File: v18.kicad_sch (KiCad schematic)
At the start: 58 parts

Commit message: More work in progres
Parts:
- added C? (x2): C, symbol Device:C
- C521, C541: renamed from C?; now not fitted
- L53, L54, L55: renamed from L?; value L_Ferrite_Power -> 100
- gave numbers to parts that had none: 53
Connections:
- net PGND is gone; now on net GNDPWR: C501.2, C502.1, C503.1, C504.2, C511.1, C512.2, C513.1, C521.2, C522.1, C523.1, C524.1, C525.1, C526.1, C527.1, C528.1, C529.1, C530.1, C541.1, C542.2, C543.2, C544.1, C545.1, C547.1, C548.1, C549.1, C550.1, C551.1, R502.2, R504.2, R521.2, R522.2, R523.2, R542.2, R543.2, U51.19 (PGND), U52.17 (NC), U52.18 (NC), U52.19 (NC), U52.21 (EP), U52.4 (6.4V), U52.5 (6.4V), U52.6 (3.2V), U52.7 (GND), U53.10 (NC), U53.11 (NC), U53.12 (NC), U53.17 (NC), U53.18 (NC), U53.19 (NC), U53.21 (EP), U53.4 (NC), U53.5 (NC), U53.6 (NC), U53.7 (GND), U53.8 (NC), U53.9 (NC)
- net at R511.1, U51.10 (COMP2): now also C?.2
- net at R501.1, U51.6 (COMP1): now also C?.2
- net GNDPWR: now reaches L52.2
- net GNDPWR: now also C?.1, C?.1
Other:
- moved on the sheet: C501, C522, C523, L53, R501, R511

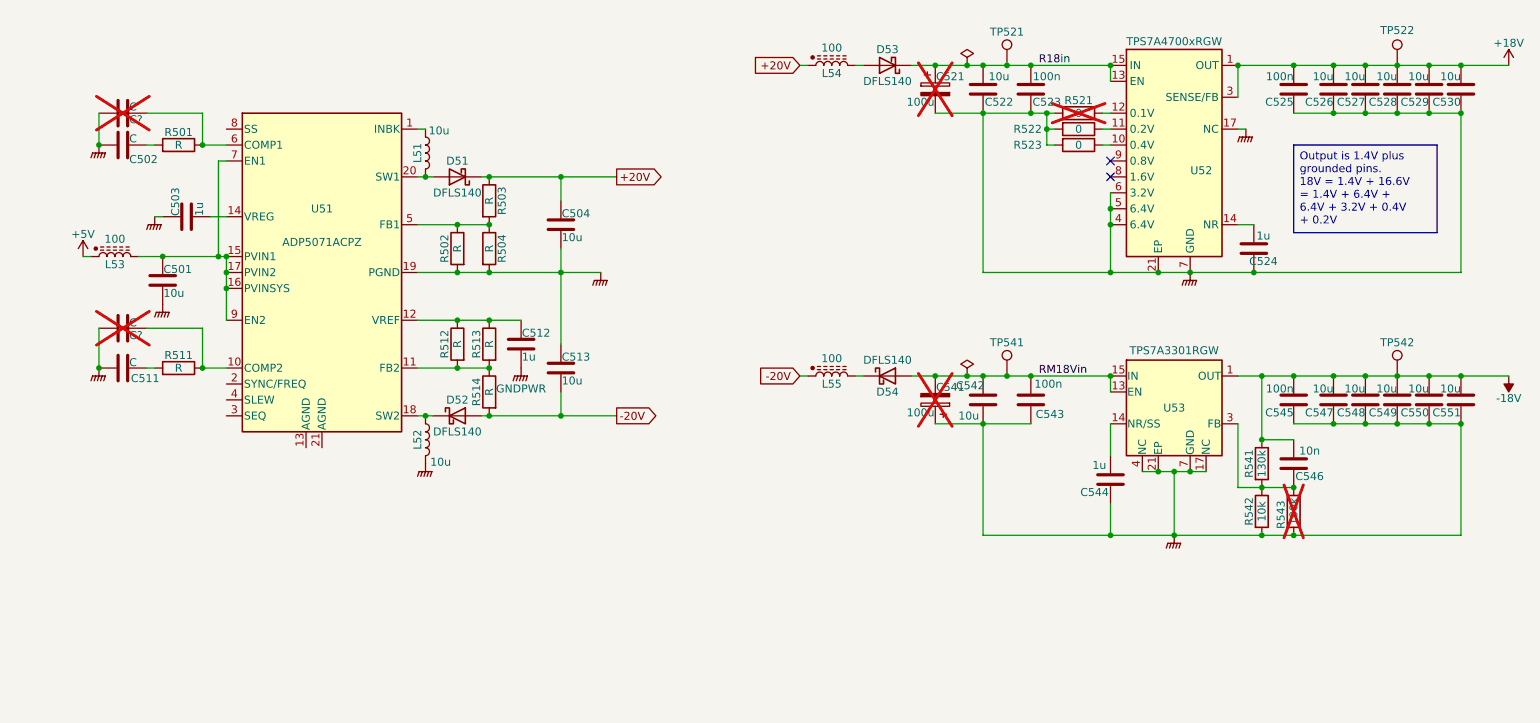
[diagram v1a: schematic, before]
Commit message: Analog side is more or less complete.
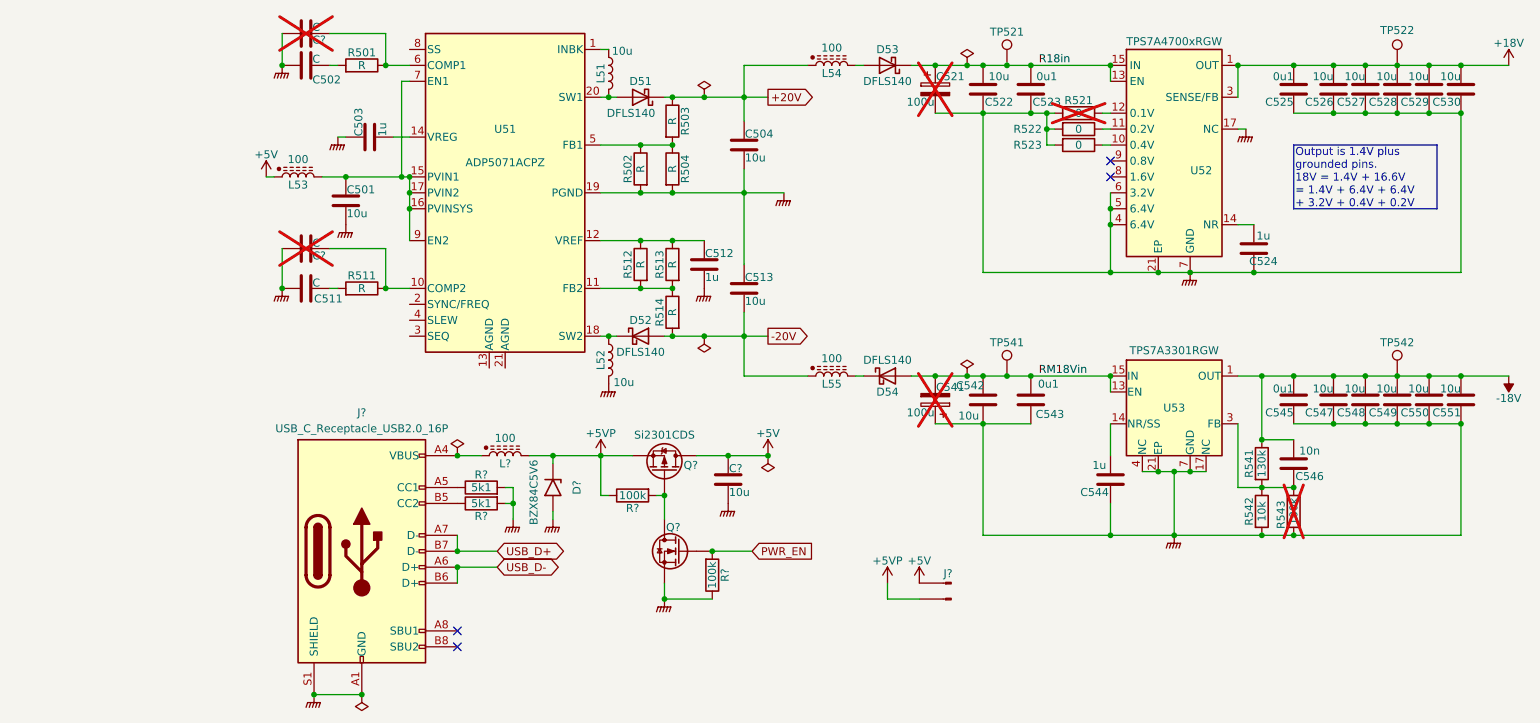
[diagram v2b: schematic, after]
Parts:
- added C?: 10u, symbol Device:C
- added D?: BZX84C5V6, Package_TO_SOT_SMD:SOT-23, symbol Parts:BZX84Cxx
- added J?: Conn_01x02_Pin, symbol Connector:Conn_01x02_Pin
- added J?: USB_C_Receptacle_USB2.0_16P, symbol Connector:USB_C_Receptacle_USB2.0_16P
- added L?: 100, symbol Parts:L_Ferrite_Power
- added Q?: Si2301CDS, Package_TO_SOT_SMD:SOT-23, symbol External:Si2301CDS
- added Q?: AO3400A, Package_TO_SOT_SMD:SOT-23, symbol Transistor_FET:AO3400A
- added R? (x2): 5k1, symbol Device:R
- added R? (x2): 100k, symbol Device:R
- C523, C525, C543, C545: value 100n -> 0u1
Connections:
- net +5V: now also C?.1, J?.2 (Pin_2), Q?.3 (D)
- net GNDPWR: now also C?.2, D?.1 (A), J?.A1 (GND), J?.A12 (GND), J?.B1 (GND), J?.B12 (GND), J?.S1 (SHIELD), Q?.2 (S), R?.1, R?.2, R?.2
- new net: Q?.1 (G), Q?.3 (D), R?.2
- new net: J?.A5 (CC1), R?.1
- new net: J?.B5 (CC2), R?.1
- new net: J?.A4 (VBUS), J?.A9 (VBUS), J?.B4 (VBUS), J?.B9 (VBUS), L?.1
- new net +5VP: D?.3 (K), J?.1 (Pin_1), L?.2, Q?.2 (S), R?.1
- new net PWR_EN: Q?.1 (G), R?.2
- new net USB_D+: J?.A7 (D-), J?.B7 (D-)
- new net USB_D-: J?.A6 (D+), J?.B6 (D+)
- no-connect marks 2 -> 4
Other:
- moved on the sheet: C501, C502, C503, C504, C511, C512, C513, C?, D51, D52, L51, L52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

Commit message: Little simplifications etc.
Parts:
- gave numbers to parts that had none: 11
- renumbered TP521 to TP51, TP522 to TP52, TP541 to TP53, TP542 to TP54
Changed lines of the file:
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@@
 		(on_board yes)
 		(dnp no)
-		(property "Reference" "TP541"
+		(property "Reference" "TP53"
 			(at 176.53 87.376 0)
 			(effects
@@
 			(project "lincal"
 				(path "/b054cef4-39e3-49d8-aff0-7ba5a206c187/79d139b8-187a-44f5-bd99-1da7793824c6"
-					(reference "TP541")
+					(reference "TP53")
 					(unit 1)
 				)
@@
 		(on_board yes)
 		(dnp no)
-		(property "Reference" "Q?"
+		(property "Reference" "Q51"
 			(at 124.968 106.934 90)
 			(effects
@@
 			(project ""
 				(path "/b054cef4-39e3-49d8-aff0-7ba5a206c187/79d139b8-187a-44f5-bd99-1da7793824c6"
-					(reference "Q?")
+					(reference "Q51")
 					(unit 1)
 				)
@@
 		(on_board yes)
 		(dnp no)
-		(property "Reference" "TP542"
+		(property "Reference" "TP54"
 			(at 238.76 87.376 0)
 			(effects
@@
 			(project "lincal"
 				(path "/b054cef4-39e3-49d8-aff0-7ba5a206c187/79d139b8-187a-44f5-bd99-1da7793824c6"
-					(reference "TP542")
+					(reference "TP54")
 					(unit 1)
 				)
@@
 		(on_board yes)
 		(dnp no)
-		(property "Reference" "R?"
+		(property "Reference" "R561"
 			(at 92.71 108.458 90)
 			(effects
@@
 			(project "lincal"
 				(path "/b054cef4-39e3-49d8-aff0-7ba5a206c187/79d139b8-187a-44f5-bd99-1da7793824c6"
-					(reference "R?")
+					(reference "R561")
 					(unit 1)
 				)
@@
 		(on_board yes)
 		(dnp no)
-		(property "Reference" "TP522"
+		(property "Reference" "TP52"
 			(at 238.76 37.592 0)
 			(effects
@@
 			(project "lincal"
 				(path "/b054cef4-39e3-49d8-aff0-7ba5a206c187/79d139b8-187a-44f5-bd99-1da7793824c6"
-					(reference "TP522")
+					(reference "TP52")
 					(unit 1)
 				)
@@
 		(on_board yes)
 		(dnp no)
-		(property "Reference" "R?"
+		(property "Reference" "R563"
 			(at 116.84 113.792 90)
 			(effects
@@
 			(project "lincal"
 				(path "/b054cef4-39e3-49d8-aff0-7ba5a206c187/79d139b8-187a-44f5-bd99-1da7793824c6"
-					(reference "R?")
+					(reference "R563")
 					(unit 1)
 				)
@@
 		(on_board yes)
 		(dnp no)
-		(property "Reference" "R?"
+		(property "Reference" "R562"
 			(at 92.71 115.062 90)
 			(effects
@@
 			(project "lincal"
 				(path "/b054cef4-39e3-49d8-aff0-7ba5a206c187/79d139b8-187a-44f5-bd99-1da7793824c6"
-					(reference "R?")
+					(reference "R562")
 					(unit 1)
 				)
@@
 		(dnp no)
 		(property "Reference" "C543"
-			(at 183.388 98.806 0)
+			(at 180.34 98.552 0)
 			(effects
 				(font
 					(size 1.27 1.27)
 				)
+				(justify right)
 			)
 		)
 		(property "Value" "0u1"
-			(at 183.134 93.98 0)
+			(at 180.34 94.488 0)
 			(effects
 				(font
 					(size 1.27 1.27)
 				)
+				(justify right)
 			)
 		)
@@
 		(on_board yes)
 		(dnp no)
-		(property "Reference" "J?"
+		(property "Reference" "J52"
 			(at 167.132 124.206 0)
 			(effects
@@
 			(project ""
 				(path "/b054cef4-39e3-49d8-aff0-7ba5a206c187/79d139b8-187a-44f5-bd99-1da7793824c6"
-					(reference "J?")
+					(reference "J52")
 					(unit 1)
 				)
@@
 		(on_board yes)
 		(dnp no)
-		(property "Reference" "D?"
+		(property "Reference" "D55"
 			(at 107.95 110.49 0)
 			(effects
@@
 			(project ""
 				(path "/b054cef4-39e3-49d8-aff0-7ba5a206c187/79d139b8-187a-44f5-bd99-1da7793824c6"
-					(reference "D?")
+					(reference "D55")
 					(unit 1)
 				)
@@
 		(dnp no)
 		(property "Reference" "C542"
-			(at 170.688 94.234 0)
+			(at 172.974 93.98 0)
 			(effects
 				(font
 					(size 1.27 1.27)
 				)
+				(justify right)
 			)
 		)
 		(property "Value" "10u"
-			(at 170.434 99.06 0)
+			(at 172.72 98.806 0)
 			(effects
 				(font
 					(size 1.27 1.27)
 				)
+				(justify right)
 			)
 		)
@@
 		(on_board yes)
 		(dnp no)
-		(property "Reference" "TP521"
+		(property "Reference" "TP51"
 			(at 176.53 37.846 0)
 			(effects
@@
 			(project "lincal"
 				(path "/b054cef4-39e3-49d8-aff0-7ba5a206c187/79d139b8-187a-44f5-bd99-1da7793824c6"
-					(reference "TP521")
+					(reference "TP51")
 					(unit 1)
 				)
@@
 		(on_board yes)
 		(dnp no)
-		(property "Reference" "J?"
+		(property "Reference" "J51"
 			(at 73.66 98.552 0)
 			(effects
@@
 			(project ""
 				(path "/b054cef4-39e3-49d8-aff0-7ba5a206c187/79d139b8-187a-44f5-bd99-1da7793824c6"
-					(reference "J?")
+					(reference "J51")
 					(unit 1)
 				)
@@
 		(on_board yes)
 		(dnp no)
-		(property "Reference" "Q?"
+		(property "Reference" "Q52"
 			(at 122.174 116.84 0)
 			(effects
@@
 			(project "lincal"
 				(path "/b054cef4-39e3-49d8-aff0-7ba5a206c187/79d139b8-187a-44f5-bd99-1da7793824c6"
-					(reference "Q?")
+					(reference "Q52")
 					(unit 1)
 				)
@@
 		(on_board yes)
 		(dnp no)
-		(property "Reference" "C?"
+		(property "Reference" "C561"
 			(at 132.207 107.442 0)
 			(effects
@@
 			(project "lincal"
 				(path "/b054cef4-39e3-49d8-aff0-7ba5a206c187/79d139b8-187a-44f5-bd99-1da7793824c6"
-					(reference "C?")
+					(reference "C561")
 					(unit 1)
 				)
@@
 		(on_board yes)
 		(dnp no)
-		(property "Reference" "R?"
+		(property "Reference" "R564"
 			(at 131.572 124.46 90)
 			(effects
@@
 			(project "lincal"
 				(path "/b054cef4-39e3-49d8-aff0-7ba5a206c187/79d139b8-187a-44f5-bd99-1da7793824c6"
-					(reference "R?")
+					(reference "R564")
 					(unit 1)
 				)
@@
 		(on_board yes)
 		(dnp no)
-		(property "Reference" "L?"
+		(property "Reference" "L56"
 			(at 96.52 106.68 90)
 			(effects
@@
 			(project "lincal"
 				(path "/b054cef4-39e3-49d8-aff0-7ba5a206c187/79d139b8-187a-44f5-bd99-1da7793824c6"
-					(reference "L?")
+					(reference "L56")
 					(unit 1)
 				)

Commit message: Schematic complete, maybe
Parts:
- removed C561: 10u, symbol Device:C
- removed D55: BZX84C5V6, Package_TO_SOT_SMD:SOT-23, symbol Parts:BZX84Cxx
- removed J51: USB_C_Receptacle_USB2.0_16P, symbol Connector:USB_C_Receptacle_USB2.0_16P
- removed J52: Conn_01x02_Pin, symbol Connector:Conn_01x02_Pin
- removed L56: 100, symbol Parts:L_Ferrite_Power
- removed Q51: Si2301CDS, Package_TO_SOT_SMD:SOT-23, symbol External:Si2301CDS
- removed Q52: AO3400A, Package_TO_SOT_SMD:SOT-23, symbol Transistor_FET:AO3400A
- removed R561, R562: 5k1, symbol Device:R
- removed R563, R564: 100k, symbol Device:R
- added C507: 0u1, Capacitor_SMD:C_0402_1005Metric, symbol Device:C
- C501: footprint (none) -> Capacitor_SMD:C_0603_1608Metric; LCSC (none) -> C96446
- C503, C512: footprint (none) -> Capacitor_SMD:C_0402_1005Metric; LCSC (none) -> C52923
- C504, C513: footprint (none) -> Capacitor_SMD:C_0805_2012Metric; LCSC (none) -> C440198
- C521, C541: now left out of the parts list
- C522, C527, C528, C529, C530, C542, C547, C548, C549, C550, C551: JLCPCB C440198 -> (none); LCSC (none) -> C440198
- C524: footprint Capacitor_SMD:C_0603_1608Metric -> Capacitor_SMD:C_0402_1005Metric; JLCPCB C15849 -> (none); LCSC (none) -> C52923
- C525, C545: JLCPCB C307331 -> (none); LCSC (none) -> C307331
- C544: JLCPCB C52923 -> (none); LCSC (none) -> C52923
- C546: footprint Capacitor_SMD:C_0402_1005Metric -> Capacitor_SMD:C_0603_1608Metric; JLCPCB C15195 -> (none); LCSC (none) -> C307500
- D51, D52, D53, D54: footprint Diode_SMD:D_SMA -> Diode_SMD:D_PowerDI-123; symbol Diode:SS34 -> Parts:DFLS140
- L53, L54, L55: footprint (none) -> Inductor_SMD:L_0603_1608Metric; LCSC (none) -> C14709
- R521, R522: footprint Parts:R_0603_Link -> Resistor_SMD:R_0603_1608Metric
- R541: JLCPCB C22795 -> (none)
- R542: JLCPCB C25744 -> (none)
- U51: LCSC (none) -> C481889
- U52: JLCPCB C114839 -> (none); LCSC (none) -> C114839; now left out of the parts list
- U53: JLCPCB C90082 -> (none); LCSC (none) -> C90082; now left out of the parts list
- gave numbers to parts that had none: 2
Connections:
- net GNDPWR: now also U51.13 (AGND), U51.21 (AGND), C507.1
- net at C501.1, L53.2, U51.15 (PVIN1)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: now also C507.2
- no-connect marks 4 -> 2
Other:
- moved on the sheet: C521, C522, C523, C524, C525, C526, C527, C528, C529, C530, C541, C542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

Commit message: Part selection
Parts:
- C522, C524, C526, C527, C528, C529, C530, C542, C547, C548, C549, C550, C551: Voltage 50V -> (none)
- C544: Voltage 25V -> (none)
- L51, L52: footprint (none) -> Inductor_SMD:L_TechFuse_SL0420; now left out of the parts list
- R521: now left out of the parts list
- R522, R523: LCSC (none) -> C21189
- R541: LCSC (none) -> C22795
- R542: LCSC (none) -> C25744
- R543: footprint Resistor_SMD:R_0603_1608Metric -> Resistor_SMD:R_0402_1005Metric; LCSC (none) -> C25741; now fitted
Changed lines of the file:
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@@
 			)
 		)
+		(property "LCSC" "C25744"
+			(at 210.82 114.3 90)
+			(effects
+				(font
+					(size 1.27 1.27)
+				)
+				(hide yes)
+			)
+		)
 		(pin "2"
 		)
@@
 			)
 		)
-		(property "Voltage" "50V"
-			(at 242.57 96.52 0)
-			(effects
-				(font
-					(size 1.27 1.27)
-				)
-				(hide yes)
-			)
-		)
 		(property "LCSC" "C440198"
 			(at 242.57 96.52 0)
@@
 			)
 		)
-		(property "Voltage" "50V"
-			(at 237.49 96.52 0)
-			(effects
-				(font
-					(size 1.27 1.27)
-				)
-				(hide yes)
-			)
-		)
 		(property "LCSC" "C440198"
 			(at 237.49 96.52 0)
@@
 			)
 		)
-		(property "Voltage" "50V"
-			(at 242.57 46.99 0)
-			(effects
-				(font
-					(size 1.27 1.27)
-				)
-				(hide yes)
-			)
-		)
 		(property "LCSC" "C440198"
 			(at 242.57 46.99 0)
@@
 			)
 		)
-		(property "Voltage" "50V"
-			(at 237.49 46.99 0)
-			(effects
-				(font
-					(size 1.27 1.27)
-				)
-				(hide yes)
-			)
-		)
 		(property "LCSC" "C440198"
 			(at 237.49 46.99 0)
@@
 			)
 		)
-		(property "Voltage" "25V"
-			(at 186.69 109.22 0)
-			(effects
-				(font
-					(size 1.27 1.27)
-				)
-				(hide yes)
-			)
-		)
 		(property "LCSC" "C52923"
 			(at 186.69 109.22 0)
@@
 		(unit 1)
 		(exclude_from_sim no)
-		(in_bom yes)
+		(in_bom no)
 		(on_board yes)
 		(dnp no)
@@
 			)
 		)
-		(property "Footprint" ""
+		(property "Footprint" "Inductor_SMD:L_TechFuse_SL0420"
 			(at 113.03 90.17 0)
 			(effects
@@
 			)
 		)
-		(property "Voltage" "50V"
-			(at 227.33 46.99 0)
-			(effects
-				(font
-					(size 1.27 1.27)
-				)
-				(hide yes)
-			)
-		)
 		(property "LCSC" "C440198"
 			(at 227.33 46.99 0)
@@
 			)
 		)
-		(property "Voltage" "50V"
-			(at 166.37 96.52 0)
-			(effects
-				(font
-					(size 1.27 1.27)
-				)
-				(hide yes)
-			)
-		)
 		(property "LCSC" "C440198"
 			(at 166.37 96.52 0)
@@
 		(unit 1)
 		(exclude_from_sim no)
-		(in_bom yes)
+		(in_bom no)
 		(on_board yes)
 		(dnp yes)
@@
 			)
 		)
-		(property "Voltage" "50V"
-			(at 222.25 46.99 0)
-			(effects
-				(font
-					(size 1.27 1.27)
-				)
-				(hide yes)
-			)
-		)
 		(property "LCSC" "C440198"
 			(at 222.25 46.99 0)
@@
 			)
 		)
-		(property "Voltage" "50V"
-			(at 222.25 96.52 0)
-			(effects
-				(font
-					(size 1.27 1.27)
-				)
-				(hide yes)
-			)
-		)
 		(property "LCSC" "C440198"
 			(at 222.25 96.52 0)
@@
 		(unit 1)
 		(exclude_from_sim no)
-		(in_bom yes)
+		(in_bom no)
 		(on_board yes)
 		(dnp no)
@@
 			)
 		)
-		(property "Footprint" ""
+		(property "Footprint" "Inductor_SMD:L_TechFuse_SL0420"
 			(at 113.03 44.45 0)
 			(effects
@@
 			)
 		)
-		(property "Voltage" "50V"
-			(at 166.37 46.99 0)
-			(effects
-				(font
-					(size 1.27 1.27)
-				)
-				(hide yes)
-			)
-		)
 		(property "LCSC" "C440198"
 			(at 166.37 46.99 0)
@@
 			)
 		)
-		(property "Voltage" "50V"
-			(at 232.41 46.99 0)
-			(effects
-				(font
-					(size 1.27 1.27)
-				)
-				(hide yes)
-			)
-		)
 		(property "LCSC" "C440198"
 			(at 232.41 46.99 0)
@@
 			)
 		)
-		(property "Voltage" "50V"
-			(at 232.41 96.52 0)
-			(effects
-				(font
-					(size 1.27 1.27)
-				)
-				(hide yes)
-			)
-		)
 		(property "LCSC" "C440198"
 			(at 232.41 96.52 0)
@@
 			)
 		)
+		(property "LCSC" "C21189"
+			(at 181.61 53.34 90)
+			(effects
+				(font
+					(size 1.27 1.27)
+				)
+				(hide yes)
+			)
+		)
 		(pin "1"
 		)
@@
 			)
 		)
-		(property "Voltage" "50V"
-			(at 209.55 72.39 0)
-			(effects
-				(font
-					(size 1.27 1.27)
-				)
-				(hide yes)
-			)
-		)
 		(property "LCSC" "C52923"
 			(at 209.55 72.39 0)
@@
 			)
 		)
+		(property "LCSC" "C21189"
+			(at 181.61 55.88 90)
+			(effects
+				(font
+					(size 1.27 1.27)
+				)
+				(hide yes)
+			)
+		)
 		(pin "1"
 		)
@@
 			)
 		)
+		(property "LCSC" "C22795"
+			(at 210.82 106.68 90)
+			(effects
+				(font
+					(size 1.27 1.27)
+				)
+				(hide yes)
+			)
+		)
 		(pin "2"
 		)
@@
 		(in_bom yes)
 		(on_board yes)
-		(dnp yes)
+		(dnp no)
 		(property "Reference" "R543"
-			(at 213.868 117.0939 90)
+			(at 213.868 114.2999 90)
 			(effects
 				(font
 					(size 1.27 1.27)
 				)
-				(justify left)
 			)
 		)
@@
 			)
 		)
-		(property "Footprint" "Resistor_SMD:R_0603_1608Metric"
+		(property "Footprint" "Resistor_SMD:R_0402_1005Metric"
 			(at 214.122 114.3 90)
 			(effects
@@
 			)
 		)
+		(property "LCSC" "C25741"
+			(at 215.9 114.3 90)
+			(effects
+				(font
+					(size 1.27 1.27)
+				)
+				(hide yes)
+			)
+		)
 		(pin "2"
 		)
@@
 			(at 227.33 96.52 0)
 			(effects
-				(font
-					(size 1.27 1.27)
-				)
-				(hide yes)
-			)
-		)
-		(property "Voltage" "50V"
-			(at 227.33 96.52 0)
-			(effects

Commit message: ERC passes.
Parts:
- removed C521, C541: 100u, symbol Device:C_Polarized
- added R505: 51k, Resistor_SMD:R_0402_1005Metric, symbol Device:R
- added R524, R544: 1, Resistor_SMD:R_0402_1005Metric, symbol Device:R
- C502: value C -> 1n; footprint (none) -> Capacitor_SMD:C_0603_1608Metric; now left out of the parts list
- C505: value C -> 3p; footprint (none) -> Capacitor_SMD:C_0603_1608Metric; now left out of the parts list
- C506: value C -> 1p5; footprint (none) -> Capacitor_SMD:C_0603_1608Metric; now left out of the parts list
- C511: value C -> 330p; footprint (none) -> Capacitor_SMD:C_0603_1608Metric; LCSC (none) -> C1664
- D51, D52: now left out of the parts list
- D53, D54: value DFLS140 -> 1N5819WS; footprint Diode_SMD:D_PowerDI-123 -> Diode_SMD:D_SOD-323; symbol Parts:DFLS140 -> Parts:1N5819WS; LCSC (none) -> C191023
- R501: value R -> 33k; footprint (none) -> Resistor_SMD:R_0603_1608Metric; LCSC (none) -> C4216
- R502: value R -> 43k; footprint (none) -> Resistor_SMD:R_0603_1608Metric; LCSC (none) -> C23172
- R503, R514: value R -> 1M; footprint (none) -> Resistor_SMD:R_0603_1608Metric; LCSC (none) -> C22935
- R504: value R -> 1M3; footprint (none) -> Resistor_SMD:R_0603_1608Metric; now left out of the parts list
- R511: value R -> 75k; footprint (none) -> Resistor_SMD:R_0603_1608Metric; LCSC (none) -> C23242
- R512: value R -> 39k; footprint (none) -> Resistor_SMD:R_0603_1608Metric; LCSC (none) -> C23153
- R513: value R -> 2M7; footprint (none) -> Resistor_SMD:R_0603_1608Metric; now left out of the parts list
- TP51, TP52, TP53, TP54: footprint Parts:TestPoint_THTPad_D1.0mm_Drill0.5mm -> Parts:TestPoint; now left out of the parts list
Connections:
- net GNDPWR: now also U51.2 (SYNC/FREQ), R505.2
- net R18in: now also R524.1; no longer D53.1 (K)
- net RM18Vin: now also R544.1; no longer D54.2 (A)
- net at U51.8 (SS): now also R505.1
- new net: D53.1 (K), R524.2
- new net: D54.2 (A), R544.2
- no-connect marks 2 -> 4
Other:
- moved on the sheet: C505

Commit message: Everything assigned except for wierd shit.
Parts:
- R524, R544: footprint Resistor_SMD:R_0402_1005Metric -> Resistor_SMD:R_0603_1608Metric; LCSC C25794 -> C22936
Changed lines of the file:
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@@
 			)
 		)
-		(property "Footprint" "Resistor_SMD:R_0402_1005Metric"
+		(property "Footprint" "Resistor_SMD:R_0603_1608Metric"
 			(at 160.02 44.958 90)
 			(effects
@@
 			)
 		)
-		(property "LCSC" "C25794"
+		(property "LCSC" "C22936"
 			(at 160.02 43.18 90)
 			(effects
@@
 			)
 		)
-		(property "Datasheet" "50V"
+		(property "Datasheet" "C0G, 50V"
 			(at 64.77 78.74 0)
 			(effects
@@
 			)
 		)
-		(property "Datasheet" "C0G, 50V"
+		(property "Datasheet" "C0G"
 			(at 64.77 43.18 0)
 			(effects
@@
 			)
 		)
-		(property "Footprint" "Resistor_SMD:R_0402_1005Metric"
+		(property "Footprint" "Resistor_SMD:R_0603_1608Metric"
 			(at 160.02 94.488 90)
 			(effects
@@
 			)
 		)
-		(property "LCSC" "C25794"
+		(property "LCSC" "C22936"
 			(at 160.02 92.71 90)
 			(effects
